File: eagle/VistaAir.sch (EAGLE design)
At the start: 6 parts

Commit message: pcb corrections
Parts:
- added J3: (no value), SparkFun-Connectors:CONN_04
- B2: device SparkFun-Boards:ESP32_THING -> kevins_parts:ESP32_THING
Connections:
- removed net GND_OUT: U$1.GND_OUT, U$2.GND_OUT
- removed net LOGIC_V: B2.3V3@36
- new net CWL2: B2.13
- new net NC1: B2.16
- new net NC2: B2.17
- net 3V6: now also J3.2; no longer B1.5V
- net BOARD_GND: now also B1.GND@0, B2.GND@1, J3.1, U$1.GND_OUT, U$2.GND_OUT; no longer B1.3.3V, B1.RES, B2.GND@37
- net CCL1: now also B1.D8, B2.26; no longer B1.SDA, B2.12
- net CCL2: now also B1.*D9, B2.25; no longer B1.SCL, B2.13
- net CLW1: now also B1.D7, B2.27; no longer B1.*D10, B2.25
- net CLW2: now also B1.D4; no longer B1.D13, B2.14
- net ENC1A: now also B2.18; no longer B2.4
- net ENC1B: now also B2.23; no longer B2.0
- net ENC2A: now also B2.4, J3.3; no longer B1.GND@0, B2.16
- net ENC2B: now also B2.0, J3.4; no longer B1.GND@1, B2.17
- net LED: now also B2.21; no longer B2.23
- net LIMBOTA: now also B2.RX; no longer B2.5
- net LIMBOTB: now also B2.TX; no longer B2.18
- net LIMTOPA: now also B2.19; no longer B2.2
- net LIMTOPB: now also B2.22; no longer B2.15
- net PWM1: now also B1.*D5, B2.12; no longer B1.D12, B2.27
- net PWM2: now also B1.*D6, B2.14; no longer B1.*D11, B2.26

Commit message: beta 1 board corrections
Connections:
- removed net CWL2: B2.13
- net CLW2: now also B2.13
- net V5IN: now also B1.5V; no longer B1.VIN
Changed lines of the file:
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@@
 <label x="68.58" y="83.82" size="1.778" layer="95"/>
+</segment>
+<segment>
+<wire x1="114.3" y1="50.8" x2="111.76" y2="53.34" width="0.1524" layer="91"/>
+<label x="106.68" y="53.34" size="1.778" layer="95"/>
+<pinref part="B2" gate="G$1" pin="13"/>
 </segment>
 </net>
@@
 </segment>
 <segment>
-<wire x1="33.02" y1="71.12" x2="25.4" y2="71.12" width="0.1524" layer="91"/>
-<label x="17.78" y="71.12" size="1.778" layer="95"/>
-<pinref part="B1" gate="G$1" pin="VIN"/>
-</segment>
-<segment>
 <wire x1="114.3" y1="38.1" x2="109.22" y2="38.1" width="0.1524" layer="91"/>
 <label x="101.6" y="38.1" size="1.778" layer="95"/>
 <pinref part="B2" gate="G$1" pin="VUSB@2"/>
 </segment>
+<segment>
+<pinref part="B1" gate="G$1" pin="5V"/>
+<wire x1="33.02" y1="68.58" x2="27.94" y2="68.58" width="0.1524" layer="91"/>
+<label x="22.86" y="68.58" size="1.778" layer="95"/>
+</segment>
 </net>
 <net name="LIMTOPA" class="0">
@@
 </segment>
 </net>
-<net name="CWL2" class="0">
-<segment>
-<wire x1="114.3" y1="50.8" x2="111.76" y2="53.34" width="0.1524" layer="91"/>
-<label x="106.68" y="53.34" size="1.778" layer="95"/>
-<pinref part="B2" gate="G$1" pin="13"/>
-</segment>
-</net>

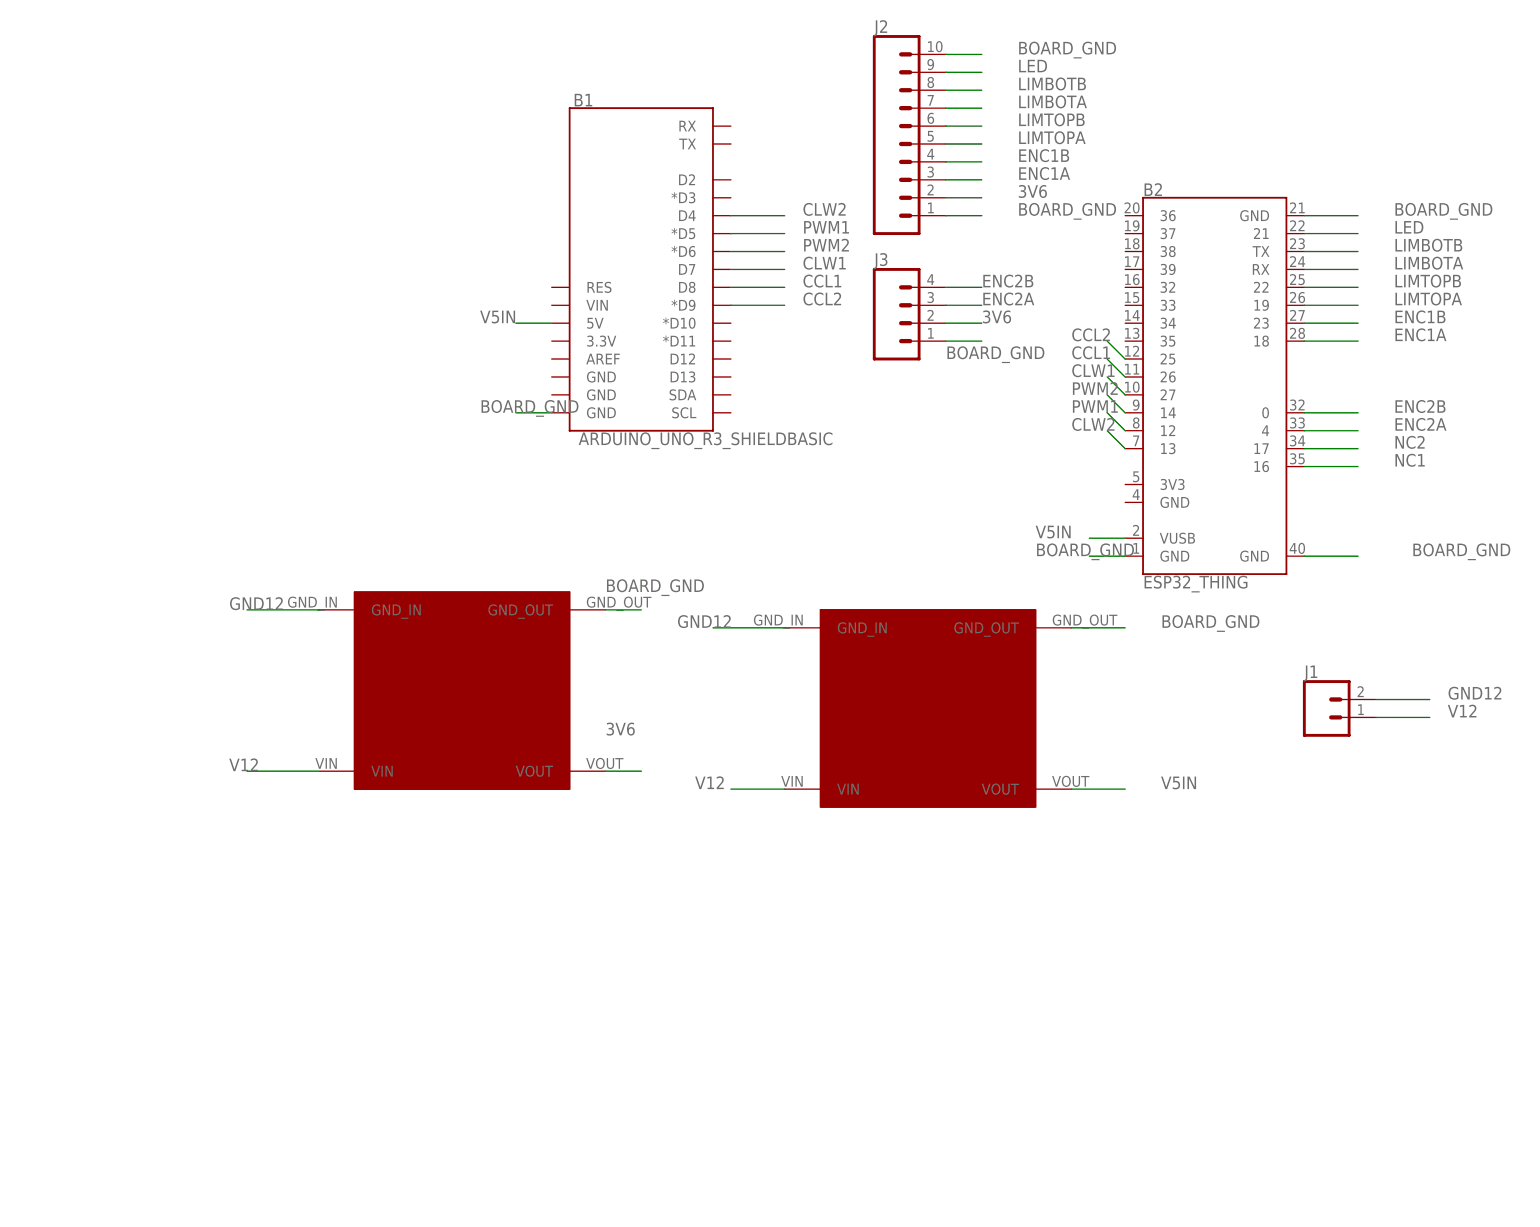
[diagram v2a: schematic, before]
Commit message: updated board for stable power - which I believe was showstopper
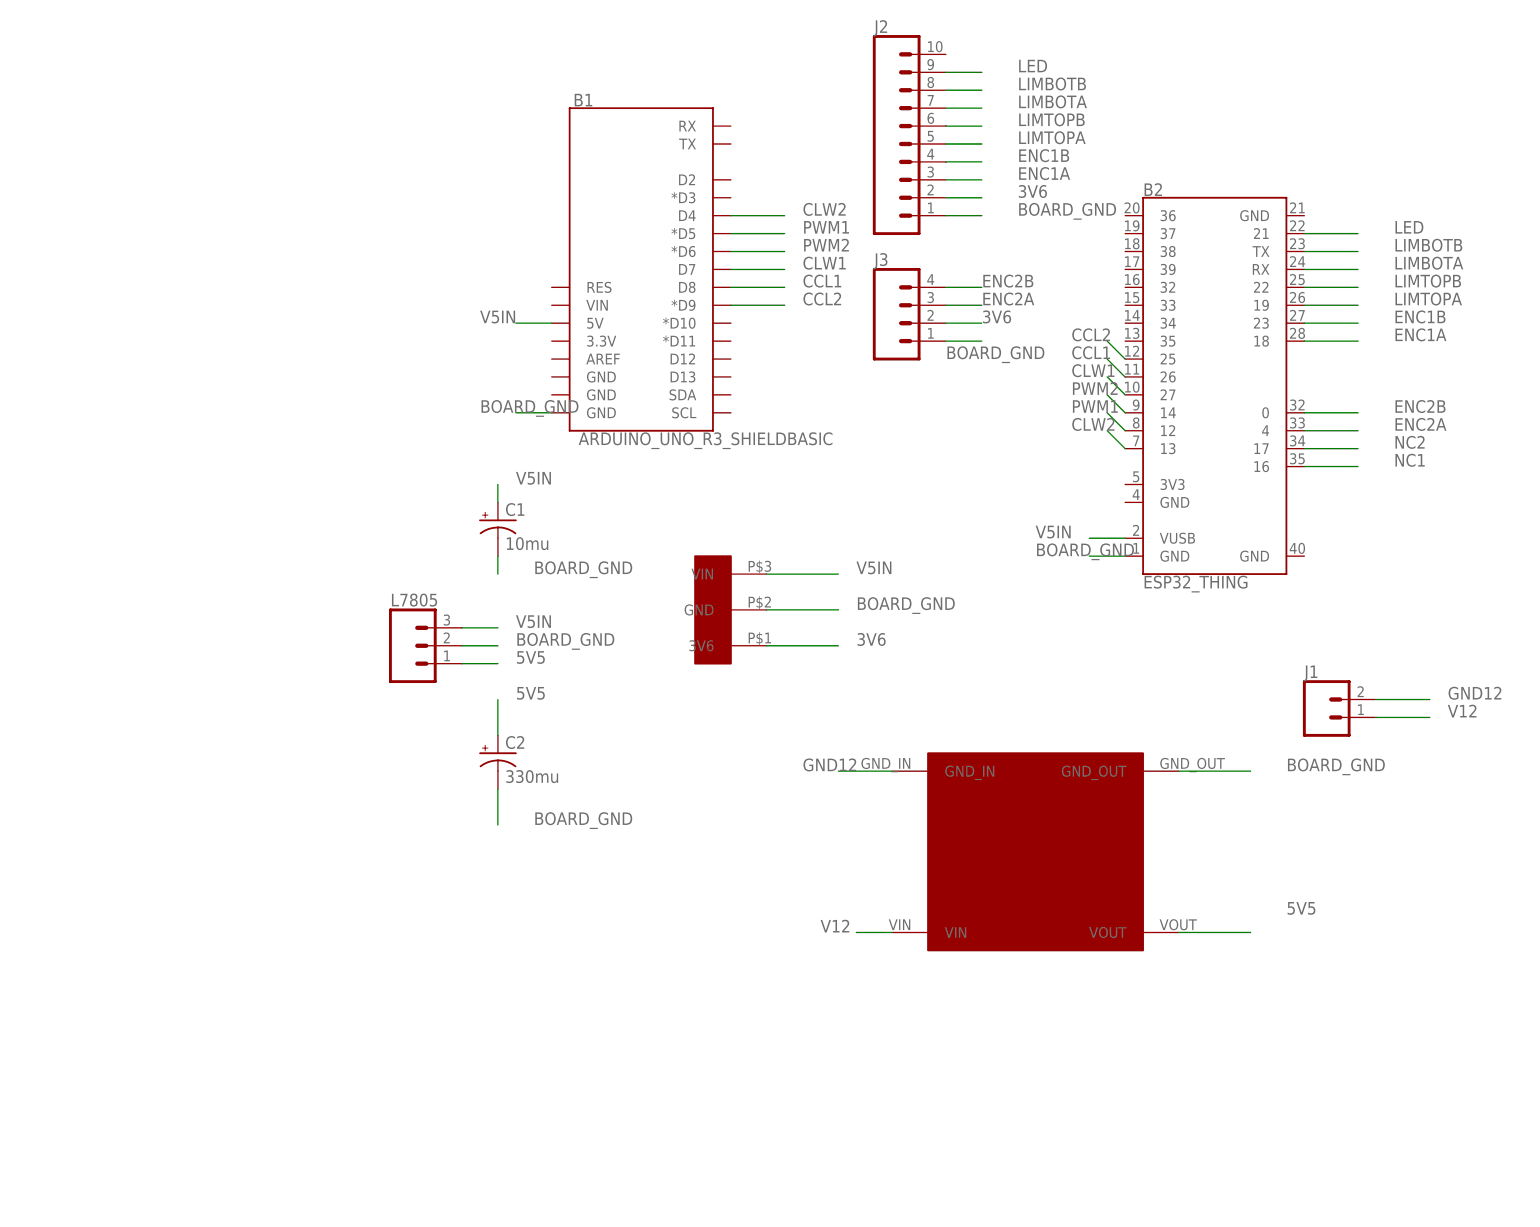
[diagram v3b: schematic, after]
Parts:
- added C1: 10mu, adafruit:CPOL-USTT2D5
- added C2: 330mu, adafruit:CPOL-USTT5D10
- added L7805: (no value), SparkFun-Connectors:CONN_03
- U$1: value MP1584EN_STEPDOWN_MODULE -> MCP1702_LDOREGULATOR; device kevins_parts:MP1584EN_STEPDOWN_MODULE -> kevins_parts:MCP1702_LDOREGULATOR
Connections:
- new net 5V5: C2.+, L7805.1, U$2.VOUT
- net 3V6: now also U$1.3V6; no longer U$2.VOUT
- net BOARD_GND: now also C1.-, C2.-, L7805.2, U$1.GND; no longer B2.GND@21, B2.GND@40, J2.10, U$1.GND_OUT
- net GND12: no longer U$1.GND_IN
- net V12: no longer U$1.VIN
- net V5IN: now also C1.+, L7805.3, U$1.VIN; no longer U$1.VOUT
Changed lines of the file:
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@@
 <layer number="230" name="230bmp" color="7" fill="1" visible="yes" active="yes"/>
 <layer number="231" name="231bmp" color="7" fill="1" visible="yes" active="yes"/>
+<layer number="232" name="Eagle3D_PG2" color="7" fill="1" visible="no" active="no"/>
+<layer number="233" name="Eagle3D_PG3" color="7" fill="1" visible="no" active="no"/>
 <layer number="248" name="Housing" color="7" fill="1" visible="yes" active="yes"/>
 <layer number="249" name="Edge" color="7" fill="1" visible="yes" active="yes"/>
@@
 <clearance class="0" value="0.508"/>
 </class>
-<class number="1" name="power" width="1.27" drill="0">
-<clearance class="1" value="1.016"/>
+<class number="1" name="power" width="0.762" drill="0">
+<clearance class="1" value="0.635"/>
 </class>
 </classes>
 <parts>
-<part name="U$1" library="kevins_parts" deviceset="MP1584EN_STEPDOWN_MODULE" device=""/>
 <part name="J1" library="SparkFun-Connectors" deviceset="CONN_02" device="PTH4"/>
 <part name="J2" library="SparkFun-Connectors" deviceset="CONN_10" device="&quot;"/>
-<part name="U$2" library="kevins_parts" deviceset="MP1584EN_STEPDOWN_MODULE" device=""/>
 <part name="B1" library="kevins_parts" deviceset="ARDUINO_UNO_R3_SHIELD" device="BASIC"/>
 <part name="B2" library="kevins_parts" deviceset="ESP32_THING" device=""/>
 <part name="J3" library="SparkFun-Connectors" deviceset="CONN_04" device=""/>
+<part name="L7805" library="SparkFun-Connectors" deviceset="CONN_03" device=""/>
+<part name="U$1" library="kevins_parts" deviceset="MCP1702_LDOREGULATOR" device=""/>
+<part name="C2" library="adafruit" deviceset="CPOL-US" device="TT5D10" value="330mu"/>
+<part name="C1" library="adafruit" deviceset="CPOL-US" device="TT2D5" value="10mu"/>
+<part name="U$2" library="kevins_parts" deviceset="MP1584EN_STEPDOWN_MODULE" device=""/>
 </parts>
 <sheets>
@@
 </plain>
 <instances>
-<instance part="U$1" gate="G$1" x="86.36" y="12.7"/>
 <instance part="J1" gate="G$1" x="142.24" y="12.7"/>
 <instance part="J2" gate="G$1" x="78.74" y="101.6"/>
-<instance part="U$2" gate="G$1" x="20.32" y="15.24"/>
 <instance part="B1" gate="G$1" x="45.72" y="78.74"/>
 <instance part="B2" gate="G$1" x="127" y="58.42"/>
 <instance part="J3" gate="G$1" x="83.82" y="68.58"/>
+<instance part="L7805" gate="J$1" x="12.7" y="22.86"/>
+<instance part="U$1" gate="G$1" x="91.44" y="20.32"/>
+<instance part="C2" gate="G$1" x="25.4" y="7.62"/>
+<instance part="C1" gate="G$1" x="25.4" y="40.64"/>
+<instance part="U$2" gate="G$1" x="101.6" y="-7.62"/>
 </instances>
 <busses>
@@
 </segment>
 </net>
-<net name="BOARD_GND" class="0">
+<net name="BOARD_GND" class="1">
 <segment>
 <pinref part="J2" gate="G$1" pin="1"/>
@@
 </segment>
 <segment>
-<wire x1="139.7" y1="35.56" x2="147.32" y2="35.56" width="0.1524" layer="91"/>
-<label x="154.94" y="35.56" size="1.778" layer="95"/>
-<pinref part="B2" gate="G$1" pin="GND@40"/>
-</segment>
-<segment>
-<pinref part="J2" gate="G$1" pin="10"/>
-<wire x1="88.9" y1="106.68" x2="93.98" y2="106.68" width="0.1524" layer="91"/>
-<label x="99.06" y="106.68" size="1.778" layer="95"/>
-</segment>
-<segment>
-<wire x1="139.7" y1="83.82" x2="147.32" y2="83.82" width="0.1524" layer="91"/>
-<label x="152.4" y="83.82" size="1.778" layer="95"/>
-<pinref part="B2" gate="G$1" pin="GND@21"/>
-</segment>
-<segment>
-<pinref part="U$2" gate="G$1" pin="GND_OUT"/>
-<wire x1="40.64" y1="27.94" x2="45.72" y2="27.94" width="0.1524" layer="91"/>
-<label x="40.64" y="30.48" size="1.778" layer="95"/>
-</segment>
-<segment>
-<pinref part="U$1" gate="G$1" pin="GND_OUT"/>
-<wire x1="106.68" y1="25.4" x2="114.3" y2="25.4" width="0.1524" layer="91"/>
-<label x="119.38" y="25.4" size="1.778" layer="95"/>
-</segment>
-<segment>
 <pinref part="J3" gate="G$1" pin="1"/>
 <wire x1="88.9" y1="66.04" x2="93.98" y2="66.04" width="0.1524" layer="91"/>
@@
 <label x="22.86" y="55.88" size="1.778" layer="95"/>
 </segment>
+<segment>
+<pinref part="U$1" gate="G$1" pin="GND"/>
+<wire x1="63.5" y1="27.94" x2="73.66" y2="27.94" width="0.1524" layer="91"/>
+<label x="76.2" y="27.94" size="1.778" layer="95"/>
+</segment>
+<segment>
+<pinref part="C1" gate="G$1" pin="-"/>
+<wire x1="25.4" y1="35.56" x2="25.4" y2="33.02" width="0.1524" layer="91"/>
+<label x="30.48" y="33.02" size="1.778" layer="95"/>
+</segment>
+<segment>
+<pinref part="C2" gate="G$1" pin="-"/>
+<wire x1="25.4" y1="2.54" x2="25.4" y2="-2.54" width="0.1524" layer="91"/>
+<label x="30.48" y="-2.54" size="1.778" layer="95"/>
+</segment>
+<segment>
+<pinref part="U$2" gate="G$1" pin="GND_OUT"/>
+<wire x1="121.92" y1="5.08" x2="132.08" y2="5.08" width="0.1524" layer="91"/>
+<label x="137.16" y="5.08" size="1.778" layer="95"/>
+</segment>
+<segment>
+<pinref part="L7805" gate="J$1" pin="2"/>
+<wire x1="20.32" y1="22.86" x2="25.4" y2="22.86" width="0.1524" layer="91"/>
+<label x="27.94" y="22.86" size="1.778" layer="95"/>
+</segment>
 </net>
 <net name="ENC2B" class="0">
@@
 <net name="V12" class="1">
 <segment>
-<pinref part="U$1" gate="G$1" pin="VIN"/>
-<wire x1="66.04" y1="2.54" x2="58.42" y2="2.54" width="0.1524" layer="91"/>
-<label x="53.34" y="2.54" size="1.778" layer="95"/>
-</segment>
-<segment>
 <pinref part="J1" gate="G$1" pin="1"/>
 <wire x1="149.86" y1="12.7" x2="157.48" y2="12.7" width="0.1524" layer="91"/>
@@
 <segment>
 <pinref part="U$2" gate="G$1" pin="VIN"/>
-<wire x1="0" y1="5.08" x2="-10.16" y2="5.08" width="0.1524" layer="91"/>
-<label x="-12.7" y="5.08" size="1.778" layer="95"/>
-</segment>
-</net>
-<net name="V5IN" class="0">
-<segment>
-<pinref part="U$1" gate="G$1" pin="VOUT"/>
-<wire x1="106.68" y1="2.54" x2="114.3" y2="2.54" width="0.1524" layer="91"/>
-<label x="119.38" y="2.54" size="1.778" layer="95"/>
-</segment>
+<wire x1="81.28" y1="-17.78" x2="76.2" y2="-17.78" width="0.1524" layer="91"/>
+<label x="71.12" y="-17.78" size="1.778" layer="95"/>
+</segment>
+</net>
+<net name="V5IN" class="1">
 <segment>
 <wire x1="114.3" y1="38.1" x2="109.22" y2="38.1" width="0.1524" layer="91"/>
@@
 <label x="22.86" y="68.58" size="1.778" layer="95"/>
 </segment>
+<segment>
+<pinref part="U$1" gate="G$1" pin="VIN"/>
+<wire x1="63.5" y1="33.02" x2="73.66" y2="33.02" width="0.1524" layer="91"/>
+<label x="76.2" y="33.02" size="1.778" layer="95"/>
+</segment>
+<segment>
+<pinref part="C1" gate="G$1" pin="+"/>
+<wire x1="25.4" y1="43.18" x2="25.4" y2="45.72" width="0.1524" layer="91"/>
+<label x="27.94" y="45.72" size="1.778" layer="95"/>
+</segment>
+<segment>
+<pinref part="L7805" gate="J$1" pin="3"/>
+<wire x1="20.32" y1="25.4" x2="25.4" y2="25.4" width="0.1524" layer="91"/>
+<label x="27.94" y="25.4" size="1.778" layer="95"/>
+</segment>
 </net>
 <net name="LIMTOPA" class="0">
@@
 <net name="GND12" class="1">
 <segment>
-<pinref part="U$2" gate="G$1" pin="GND_IN"/>
-<wire x1="0" y1="27.94" x2="-10.16" y2="27.94" width="0.1524" layer="91"/>
-<label x="-12.7" y="27.94" size="1.778" layer="95"/>
-</segment>
-<segment>
-<pinref part="U$1" gate="G$1" pin="GND_IN"/>
-<wire x1="66.04" y1="25.4" x2="55.88" y2="25.4" width="0.1524" layer="91"/>
-<label x="50.8" y="25.4" size="1.778" layer="95"/>
-</segment>
-<segment>
 <pinref part="J1" gate="G$1" pin="2"/>
 <wire x1="149.86" y1="15.24" x2="157.48" y2="15.24" width="0.1524" layer="91"/>
 <label x="160.02" y="15.24" size="1.778" layer="95"/>
 </segment>
+<segment>
+<pinref part="U$2" gate="G$1" pin="GND_IN"/>
+<wire x1="81.28" y1="5.08" x2="73.66" y2="5.08" width="0.1524" layer="91"/>
+<label x="68.58" y="5.08" size="1.778" layer="95"/>
+</segment>
 </net>
 <net name="3V6" class="0">
-<segment>
-<pinref part="U$2" gate="G$1" pin="VOUT"/>
-<wire x1="40.64" y1="5.08" x2="45.72" y2="5.08" width="0.1524" layer="91"/>
-<label x="40.64" y="10.16" size="1.778" layer="95"/>
-</segment>
 <segment>
 <pinref part="J2" gate="G$1" pin="2"/>
@@
 <label x="93.98" y="68.58" size="1.778" layer="95"/>
 </segment>
+<segment>
+<pinref part="U$1" gate="G$1" pin="3V6"/>
+<wire x1="63.5" y1="22.86" x2="73.66" y2="22.86" width="0.1524" layer="91"/>
+<label x="76.2" y="22.86" size="1.778" layer="95"/>
+</segment>
 </net>
 <net name="NC1" class="0">
@@
 </segment>
 </net>
+<net name="5V5" class="1">
+<segment>
+<pinref part="C2" gate="G$1" pin="+"/>
+<wire x1="25.4" y1="10.16" x2="25.4" y2="15.24" width="0.1524" layer="91"/>
+<label x="27.94" y="15.24" size="1.778" layer="95"/>
+</segment>
+<segment>
+<pinref part="U$2" gate="G$1" pin="VOUT"/>
+<wire x1="121.92" y1="-17.78" x2="132.08" y2="-17.78" width="0.1524" layer="91"/>
+<label x="137.16" y="-15.24" size="1.778" layer="95"/>
+</segment>
+<segment>
+<pinref part="L7805" gate="J$1" pin="1"/>
+<wire x1="20.32" y1="20.32" x2="25.4" y2="20.32" width="0.1524" layer="91"/>
+<label x="27.94" y="20.32" size="1.778" layer="95"/>
+</segment>
+</net>
